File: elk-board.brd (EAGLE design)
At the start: 55 x 25.6 mm, 201 parts, among them IC1 KLM8G1GESD-B03P, IC10 MP2143DJ-LF-P, IC2 ALLWINNER--H3, IC3 SY6280, IC4 K4B4G1646B-BCK0, IC5 RT8059GJ5, IC6 RT8059GJ5, IC7 SY8089A, IC8 NCP803SN263T1G, IC9 RT8059GJ5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

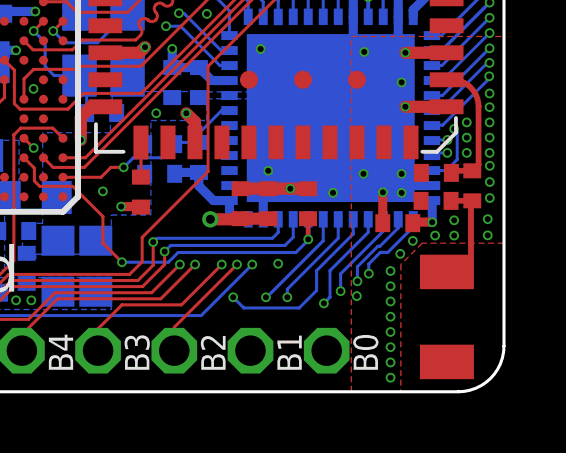
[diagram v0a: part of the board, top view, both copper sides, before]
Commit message: Moved the Antenna a little bit
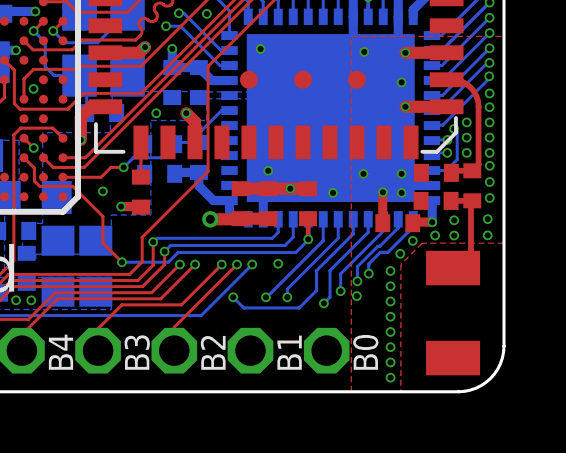
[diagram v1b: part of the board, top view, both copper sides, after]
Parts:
- moved ANT1 0.24 mm to (53.3, 2.62)
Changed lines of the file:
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@@
 <layers>
 <layer number="1" name="Top" color="4" fill="1" visible="yes" active="yes"/>
-<layer number="2" name="GND1" color="62" fill="1" visible="yes" active="yes"/>
+<layer number="2" name="GND1" color="62" fill="1" visible="no" active="yes"/>
 <layer number="3" name="SIG1_RAM" color="42" fill="1" visible="no" active="yes"/>
-<layer number="4" name="GND2" color="63" fill="1" visible="yes" active="yes"/>
+<layer number="4" name="GND2" color="63" fill="1" visible="no" active="yes"/>
 <layer number="5" name="Route5" color="19" fill="1" visible="no" active="no"/>
 <layer number="6" name="Route6" color="25" fill="1" visible="no" active="no"/>
@@
 <layer number="11" name="Route11" color="30" fill="1" visible="no" active="no"/>
 <layer number="12" name="Route12" color="20" fill="1" visible="no" active="no"/>
-<layer number="13" name="PWR" color="16" fill="1" visible="yes" active="yes"/>
+<layer number="13" name="PWR" color="16" fill="1" visible="no" active="yes"/>
 <layer number="14" name="SIG2_RAM" color="22" fill="1" visible="no" active="yes"/>
-<layer number="15" name="GND3" color="21" fill="1" visible="yes" active="yes"/>
-<layer number="16" name="Bottom" color="1" fill="1" visible="no" active="yes"/>
+<layer number="15" name="GND3" color="21" fill="1" visible="no" active="yes"/>
+<layer number="16" name="Bottom" color="1" fill="1" visible="yes" active="yes"/>
 <layer number="17" name="Pads" color="2" fill="1" visible="yes" active="yes"/>
 <layer number="18" name="Vias" color="2" fill="1" visible="yes" active="yes"/>
@@
 <layer number="22" name="bPlace" color="7" fill="1" visible="no" active="yes"/>
 <layer number="23" name="tOrigins" color="15" fill="1" visible="yes" active="yes"/>
-<layer number="24" name="bOrigins" color="15" fill="1" visible="no" active="yes"/>
+<layer number="24" name="bOrigins" color="15" fill="1" visible="yes" active="yes"/>
 <layer number="25" name="tNames" color="7" fill="1" visible="yes" active="yes"/>
 <layer number="26" name="bNames" color="7" fill="1" visible="no" active="yes"/>
@@
 <attribute name="NAME" x="53.92725" y="5.52755" size="0.6096" layer="138" font="vector" ratio="15" rot="R270" align="center"/>
 </element>
-<element name="ANT1" library="AMCA31-2R450G-S1F-T3" package="ANTC3216X140N" value="AMCA31-2R450G-S1F-T3" x="53.0987" y="2.49555" smashed="yes" rot="R270">
-<attribute name="DESCRIPTION" value="ABRACON - AMCA31-2R450G-S1F-T3 - ANTENNA, CHIP, 2.45GHZ, 50 OHM, 1206" x="53.0987" y="2.49555" size="1.778" layer="27" rot="R270" display="off"/>
-<attribute name="HEIGHT" value="1.4mm" x="53.0987" y="2.49555" size="1.778" layer="27" rot="R270" display="off"/>
-<attribute name="MANUFACTURER_NAME" value="ABRACON" x="53.0987" y="2.49555" size="1.778" layer="27" rot="R270" display="off"/>
-<attribute name="MANUFACTURER_PART_NUMBER" value="AMCA31-2R450G-S1F-T3" x="53.0987" y="2.49555" size="1.778" layer="27" rot="R270" display="off"/>
-<attribute name="MOUSER_PART_NUMBER" value="815-CA312R450GS1FT3" x="53.0987" y="2.49555" size="1.778" layer="27" rot="R270" display="off"/>
-<attribute name="MOUSER_PRICE-STOCK" value="https://www.mouser.com/Search/Refine.aspx?Keyword=815-CA312R450GS1FT3" x="53.0987" y="2.49555" size="1.778" layer="27" rot="R270" display="off"/>
-<attribute name="NAME" x="51.7017" y="2.49555" size="0.6096" layer="138" rot="R270" align="center"/>
-<attribute name="RS_PART_NUMBER" value="" x="53.0987" y="2.49555" size="1.778" layer="27" rot="R270" display="off"/>
-<attribute name="RS_PRICE-STOCK" value="" x="53.0987" y="2.49555" size="1.778" layer="27" rot="R270" display="off"/>
+<element name="ANT1" library="AMCA31-2R450G-S1F-T3" package="ANTC3216X140N" value="AMCA31-2R450G-S1F-T3" x="53.3019" y="2.62255" smashed="yes" rot="R270">
+<attribute name="DESCRIPTION" value="ABRACON - AMCA31-2R450G-S1F-T3 - ANTENNA, CHIP, 2.45GHZ, 50 OHM, 1206" x="53.3019" y="2.62255" size="1.778" layer="27" rot="R270" display="off"/>
+<attribute name="HEIGHT" value="1.4mm" x="53.3019" y="2.62255" size="1.778" layer="27" rot="R270" display="off"/>
+<attribute name="MANUFACTURER_NAME" value="ABRACON" x="53.3019" y="2.62255" size="1.778" layer="27" rot="R270" display="off"/>
+<attribute name="MANUFACTURER_PART_NUMBER" value="AMCA31-2R450G-S1F-T3" x="53.3019" y="2.62255" size="1.778" layer="27" rot="R270" display="off"/>
+<attribute name="MOUSER_PART_NUMBER" value="815-CA312R450GS1FT3" x="53.3019" y="2.62255" size="1.778" layer="27" rot="R270" display="off"/>
+<attribute name="MOUSER_PRICE-STOCK" value="https://www.mouser.com/Search/Refine.aspx?Keyword=815-CA312R450GS1FT3" x="53.3019" y="2.62255" size="1.778" layer="27" rot="R270" display="off"/>
+<attribute name="NAME" x="51.9049" y="2.62255" size="0.6096" layer="138" rot="R270" align="center"/>
+<attribute name="RS_PART_NUMBER" value="" x="53.3019" y="2.62255" size="1.778" layer="27" rot="R270" display="off"/>
+<attribute name="RS_PRICE-STOCK" value="" x="53.3019" y="2.62255" size="1.778" layer="27" rot="R270" display="off"/>
 </element>
 <element name="C27" library="GHI-BasicComponents" package="0402" value="" x="52.73675" y="6.3627" smashed="yes">
@@
 <wire x1="53.94325" y1="6.36435" x2="53.8988" y2="6.3199" width="0.193040625" layer="1"/>
 <wire x1="53.8988" y1="6.3199" x2="53.8988" y2="4.41465" width="0.193040625" layer="1"/>
-<wire x1="53.8988" y1="4.41465" x2="53.4797" y2="3.99555" width="0.193040625" layer="1"/>
-<wire x1="53.4797" y1="3.99555" x2="53.0987" y2="3.99555" width="0.193040625" layer="1"/>
+<wire x1="53.8988" y1="4.41465" x2="53.6067" y2="4.12255" width="0.193040625" layer="1"/>
+<wire x1="53.6067" y1="4.12255" x2="53.3019" y2="4.12255" width="0.193040625" layer="1"/>
 </signal>
 <signal name="N$27">

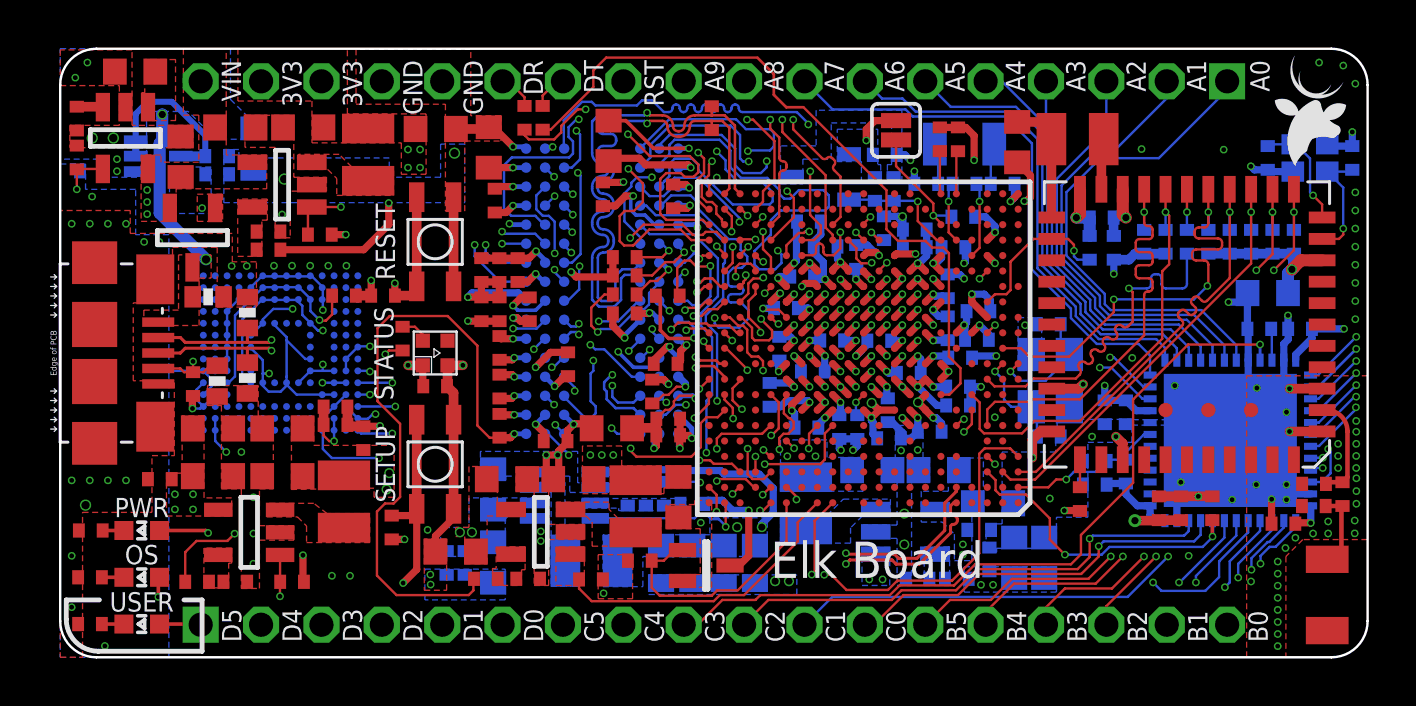
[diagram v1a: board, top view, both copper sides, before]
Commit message: Added and Modified GND vias and increased eMMC CLK length and it's clearance with nearby traces
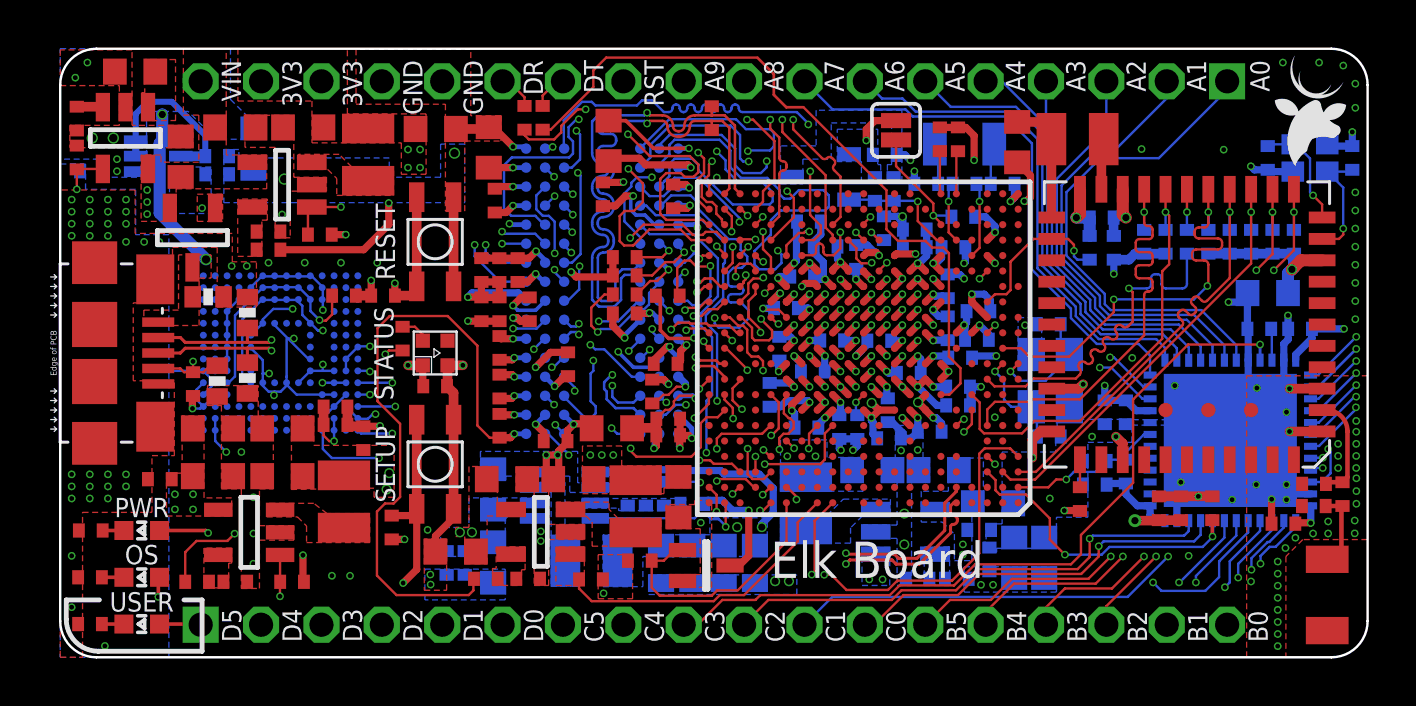
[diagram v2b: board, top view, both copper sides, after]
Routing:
- net EMMC_CLK: track 36.4 -> 41.6 mm
- net USB0_DRVVBUS: track 43.9 -> 44.5 mm
- net GND: track 198.6 -> 199.0 mm, vias 200 -> 220

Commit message: Added Some GND vias and moved USB_DRVVBUS via position
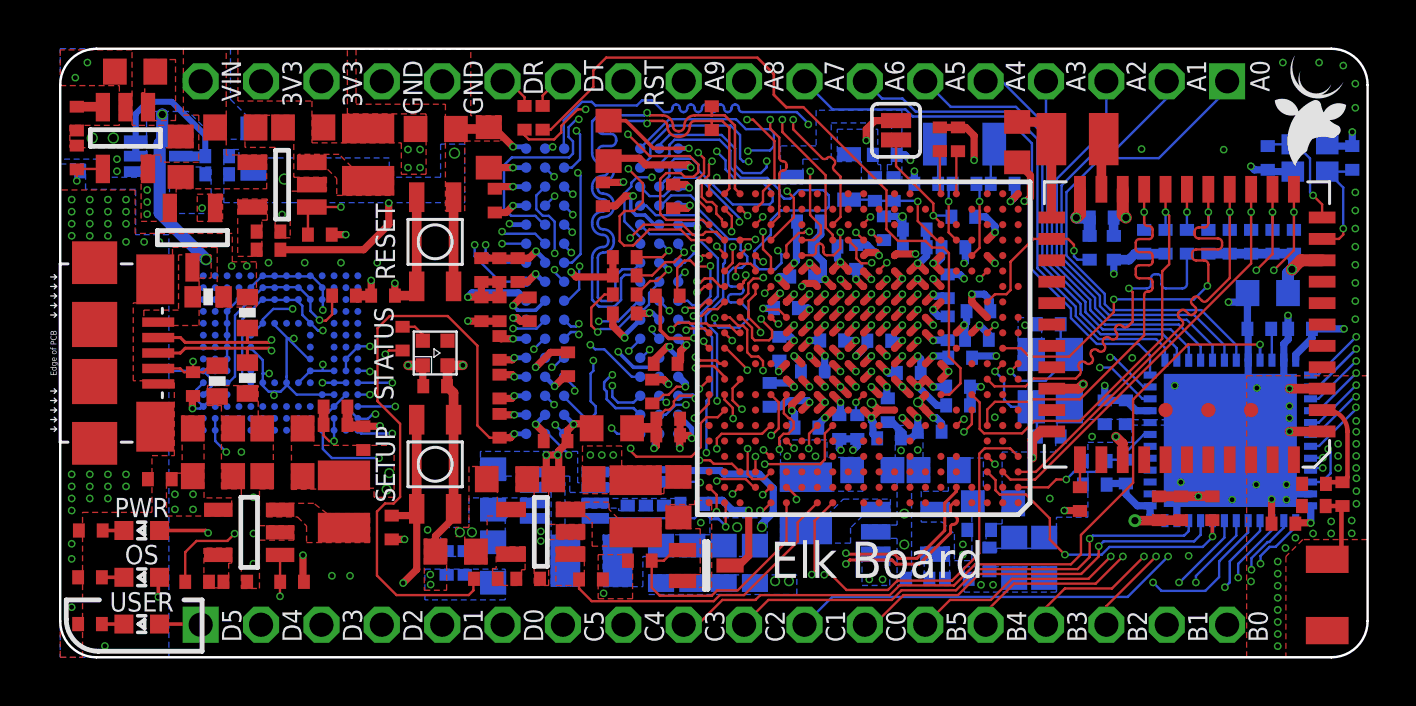
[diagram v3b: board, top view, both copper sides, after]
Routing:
- net USB0_DRVVBUS: track 44.5 -> 44.0 mm
- net GND: vias 220 -> 223
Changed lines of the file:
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@@
 <setting verticaltext="up"/>
 </settings>
-<grid distance="20" unitdist="mil" unit="mil" style="lines" multiple="1" display="no" altdistance="1" altunitdist="mil" altunit="mil"/>
+<grid distance="5" unitdist="mil" unit="mil" style="lines" multiple="1" display="no" altdistance="1" altunitdist="mil" altunit="mil"/>
 <layers>
 <layer number="1" name="Top" color="4" fill="1" visible="yes" active="yes"/>
@@
 <layer number="20" name="Dimension" color="24" fill="1" visible="yes" active="yes"/>
 <layer number="21" name="tPlace" color="7" fill="1" visible="yes" active="yes"/>
-<layer number="22" name="bPlace" color="7" fill="1" visible="yes" active="yes"/>
+<layer number="22" name="bPlace" color="7" fill="1" visible="no" active="yes"/>
 <layer number="23" name="tOrigins" color="15" fill="1" visible="yes" active="yes"/>
 <layer number="24" name="bOrigins" color="15" fill="1" visible="yes" active="yes"/>
@@
 <layer number="50" name="dxf" color="7" fill="1" visible="no" active="no"/>
 <layer number="51" name="tDocu" color="7" fill="1" visible="yes" active="yes"/>
-<layer number="52" name="bDocu" color="7" fill="1" visible="yes" active="yes"/>
+<layer number="52" name="bDocu" color="7" fill="1" visible="no" active="yes"/>
 <layer number="53" name="tGND_GNDA" color="7" fill="9" visible="no" active="no"/>
 <layer number="54" name="bGND_GNDA" color="1" fill="9" visible="no" active="no"/>
@@
 <wire x1="19.6" y1="14.2" x2="19.127" y2="14.2" width="0.2032" layer="16"/>
 <wire x1="19.127" y1="14.2" x2="19.05" y2="14.277" width="0.2032" layer="16"/>
-<via x="0.4826" y="4.2672" extent="1-16" drill="0.2"/>
+<via x="0.4826" y="4.7752" extent="1-16" drill="0.2"/>
 <via x="0.4826" y="2.1082" extent="1-16" drill="0.2"/>
 <via x="0.635" y="24.384" extent="1-16" drill="0.2"/>
@@
 <via x="51.587" y="7.2644" extent="1-16" drill="0.2"/>
 <via x="50.317" y="7.2644" extent="1-16" drill="0.2"/>
-<via x="51.587" y="10.3124" extent="1-16" drill="0.2"/>
+<via x="51.714" y="10.5664" extent="1-16" drill="0.2"/>
 <via x="50.3424" y="11.3284" extent="1-16" drill="0.2"/>
 <via x="50.09515" y="3.19" extent="1-16" drill="0.2"/>
@@
 <via x="51.2191" y="4.0259" extent="1-16" drill="0.2"/>
 <via x="51.54295" y="4.5974" extent="1-16" drill="0.2"/>
-<via x="54.4576" y="5.7531" extent="1-16" drill="0.2"/>
+<via x="54.3306" y="5.7531" extent="1-16" drill="0.2"/>
 <via x="54.52745" y="6.45795" extent="1-16" drill="0.2"/>
 <via x="54.52745" y="6.99135" extent="1-16" drill="0.2"/>
 <via x="54.52745" y="7.5311" extent="1-16" drill="0.2"/>
-<via x="53.34" y="5.207" extent="1-16" drill="0.2"/>
-<via x="53.34" y="5.715" extent="1-16" drill="0.2"/>
-<via x="54.4576" y="5.21335" extent="1-16" drill="0.2"/>
+<via x="53.467" y="5.207" extent="1-16" drill="0.2"/>
+<via x="53.467" y="5.715" extent="1-16" drill="0.2"/>
+<via x="54.3306" y="5.21335" extent="1-16" drill="0.2"/>
 <via x="51.96205" y="5.0292" extent="1-16" drill="0.2"/>
 <via x="51.587" y="6.6294" extent="1-16" drill="0.2"/>
@@
 <via x="54.483" y="23.114" extent="1-16" drill="0.2"/>
 <via x="51.435" y="25.019" extent="1-16" drill="0.2"/>
+<via x="0.4826" y="6.1722" extent="1-16" drill="0.2"/>
+<via x="0.4826" y="4.1402" extent="1-16" drill="0.2"/>
+<via x="51.714" y="10.0584" extent="1-16" drill="0.2"/>
 </signal>
 <signal name="N$1" class="9">
@@
 <wire x1="0.6985" y1="20.544" x2="1.795" y2="20.544" width="0.1016" layer="1"/>
 <via x="30.972" y="6.6368" extent="1-16" drill="0.2"/>
-<wire x1="0.6985" y1="20.526" x2="0.6985" y2="19.685" width="0.1016" layer="1"/>
-<via x="0.6985" y="19.685" extent="1-16" drill="0.2"/>
-<wire x1="4.0259" y1="20.0406" x2="1.0541" y2="20.0406" width="0.1016" layer="3"/>
-<wire x1="0.6985" y1="19.685" x2="1.0541" y2="20.0406" width="0.1016" layer="3"/>
+<wire x1="0.6985" y1="20.526" x2="0.6985" y2="20.0406" width="0.1016" layer="1"/>
+<via x="0.6985" y="20.0406" extent="1-16" drill="0.2"/>
 <wire x1="4.7879" y1="19.2786" x2="4.0259" y2="20.0406" width="0.1016" layer="3"/>
 <wire x1="4.7879" y1="19.2786" x2="4.7879" y2="9.6901" width="0.1016" layer="3"/>
@@
 <wire x1="14.716015625" y1="8.721615625" x2="8.778984375" y2="8.721615625" width="0.1016" layer="3"/>
 <wire x1="8.778984375" y1="8.721615625" x2="8.509" y2="8.9916" width="0.1016" layer="3"/>
+<wire x1="4.0259" y1="20.0406" x2="0.6985" y2="20.0406" width="0.1016" layer="3"/>
 </signal>
 <signal name="N$46">

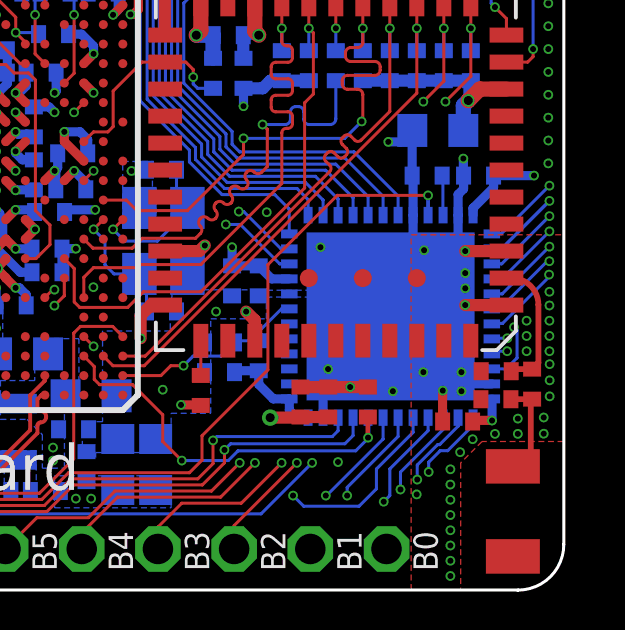
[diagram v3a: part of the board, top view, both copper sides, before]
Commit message: Changed the RAM part Number in the schematic and modified the Wifi module label
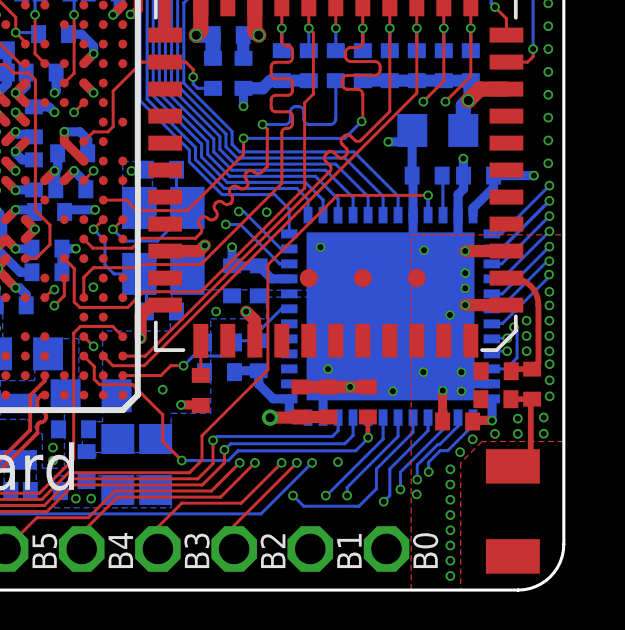
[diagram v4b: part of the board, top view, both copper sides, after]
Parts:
- IC4: value K4B4G1646B-BCK0 -> K4B4G1646D-BCK0
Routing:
- net GND: vias 223 -> 224
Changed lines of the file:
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@@
 <attribute name="NAME" x="18.54915" y="17.686" size="0.6096" layer="138" font="vector" ratio="15" rot="MR270" align="center"/>
 </element>
-<element name="IC4" library="K4B4G1646B-BCK0" package="BGA96C80P9X16_1000X1330X120" value="K4B4G1646B-BCK0" x="22.8" y="15.4" smashed="yes" rot="MR180">
+<element name="IC4" library="K4B4G1646B-BCK0" package="BGA96C80P9X16_1000X1330X120" value="K4B4G1646D-BCK0" x="22.8" y="15.4" smashed="yes" rot="MR180">
 <attribute name="DESCRIPTION" value="4Gb B-die DDR3 SDRAM" x="82.49" y="23.02" size="1.778" layer="28" rot="MR180" display="off"/>
 <attribute name="HEIGHT" value="1.2mm" x="82.49" y="23.02" size="1.778" layer="28" rot="MR180" display="off"/>
@@
 <via x="0.4826" y="4.1402" extent="1-16" drill="0.2"/>
 <via x="51.714" y="10.0584" extent="1-16" drill="0.2"/>
+<via x="51.206" y="9.1694" extent="1-16" drill="0.2"/>
 </signal>
 <signal name="N$1" class="9">
